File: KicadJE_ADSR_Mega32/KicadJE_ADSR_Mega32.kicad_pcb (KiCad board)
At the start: 2 copper layers, 100 x 100 mm, 134 parts, among them J101 ADSR1, J102 ADSR2, J103 ADSR1, J104 ADSR2, J105 ADSR1-G8, J106 ADSR2-G8, J107 ADSR4-G8, J108 ADSR3-G8, J201 AVR-ISP-6, J202 UART, J301 In, J302 +5V reg/doepfer, J303 Out, J304 CV_time, J305 CV doepfer, P101 Doepfer_Power_16pin, P302 Doepfer_Power_16pin, Q301 BC337, Q302 PZT2222A, U201 ATmega32A-AU, U301 L78L05_TO92, U302 PT2399, Y201 16MHz

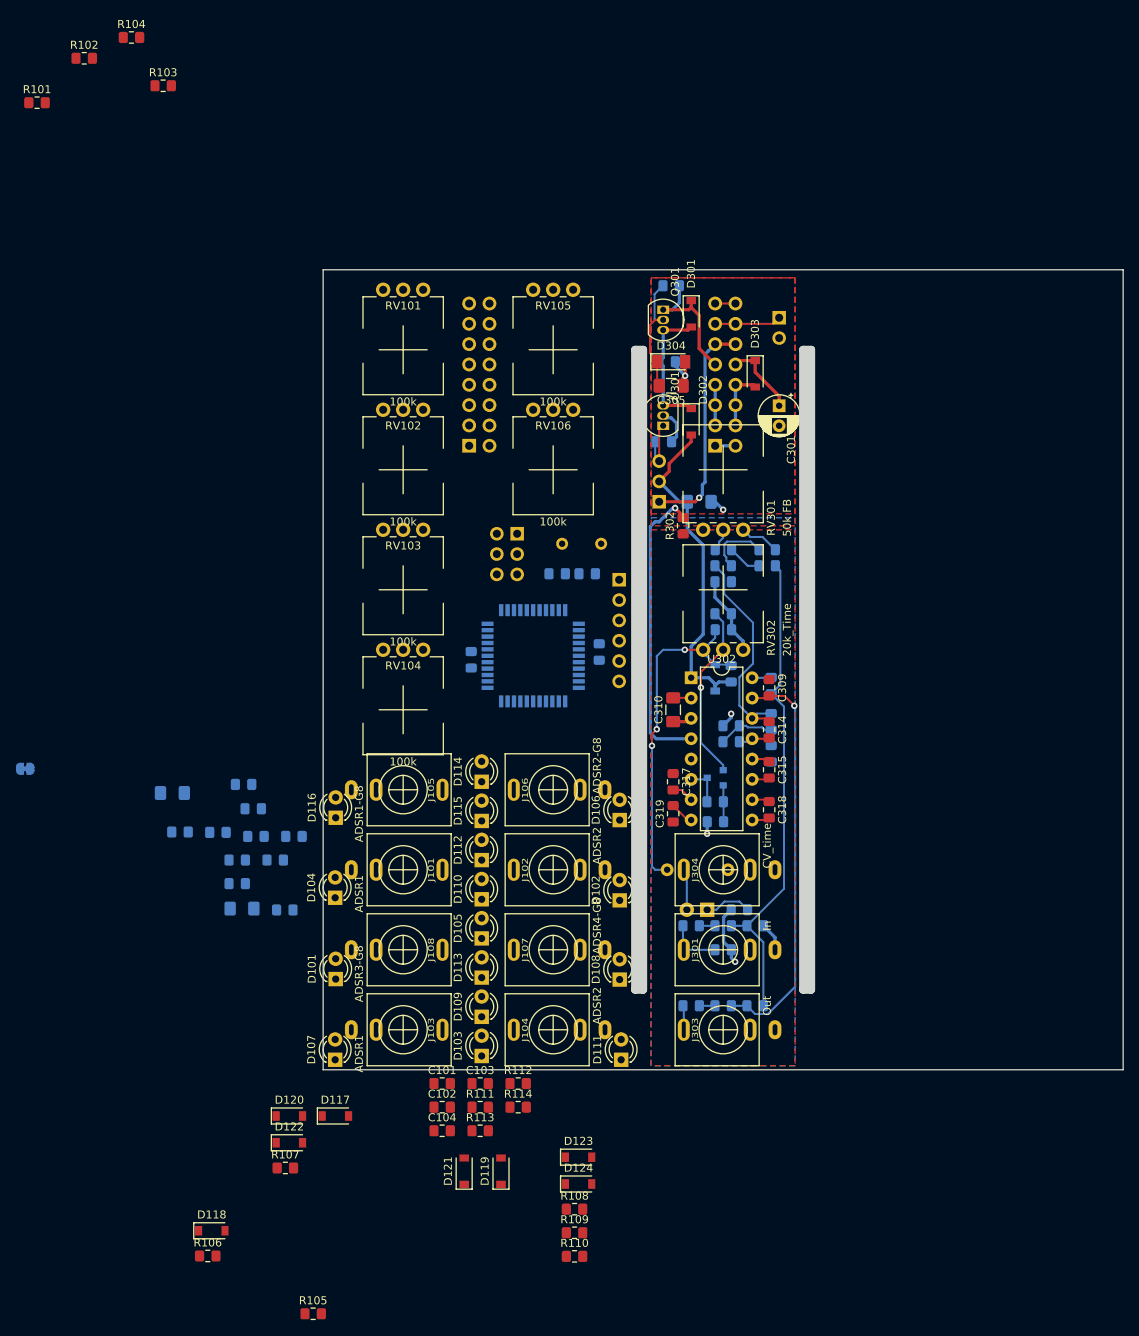
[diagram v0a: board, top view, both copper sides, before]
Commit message: Alternative pull down
Pull down via 10k but connected via TN - so if no input is applied they are connected via Gate input. This enables sync gate
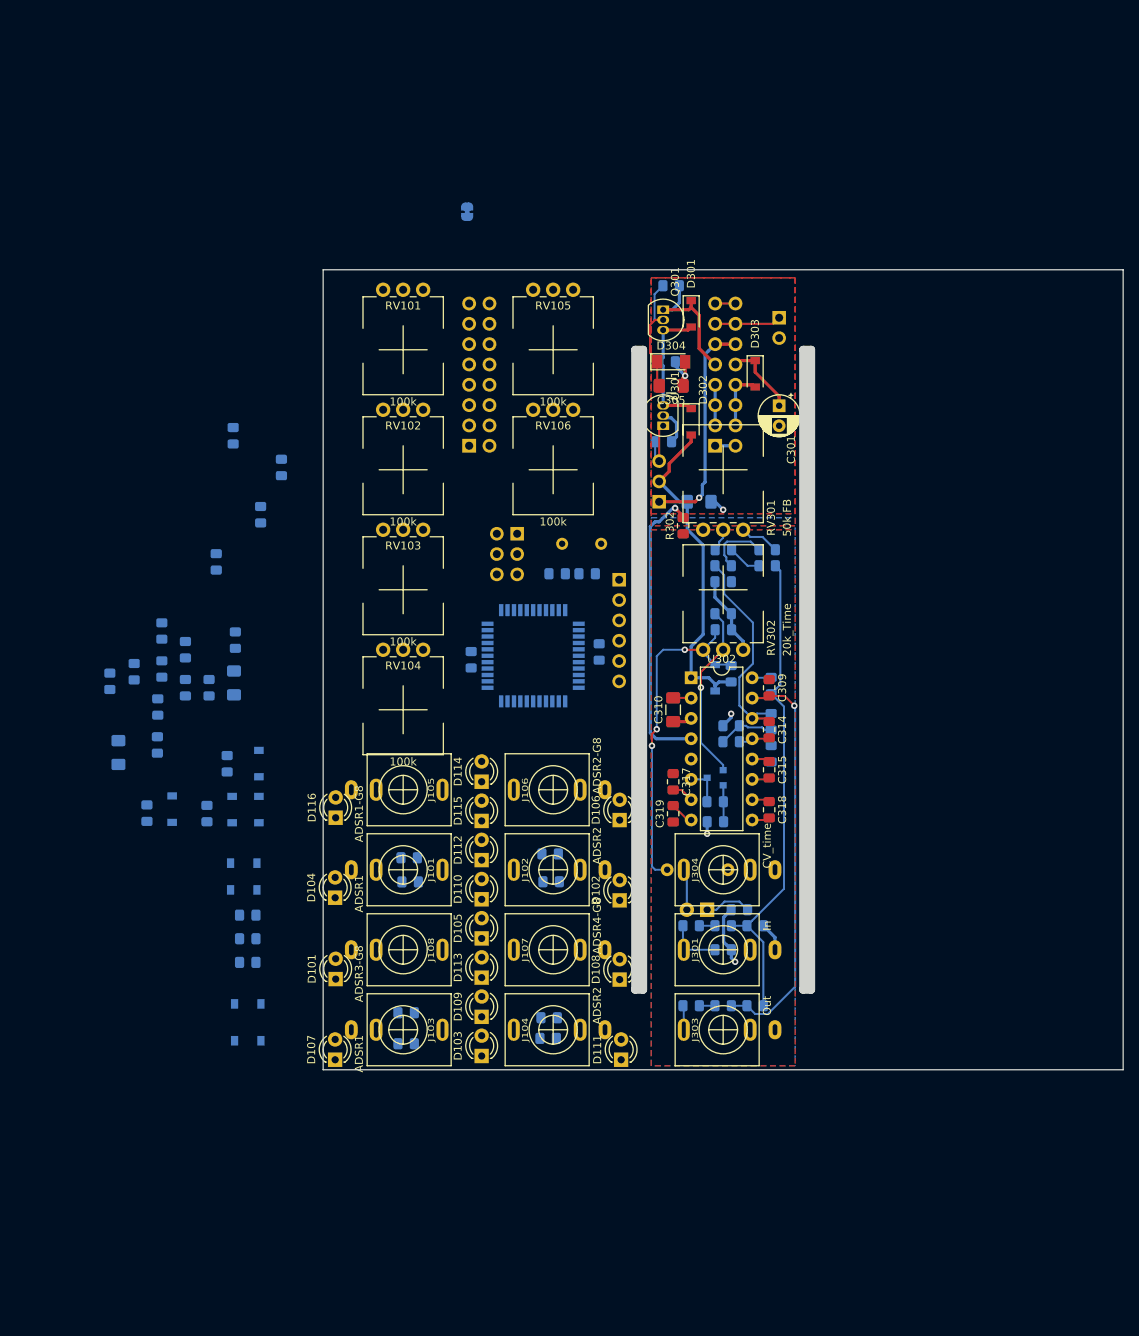
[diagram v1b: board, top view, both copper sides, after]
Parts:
- C101, C102, C103, C104, D117, D118, D119, D120, D121, D122, D123, D124, R101, R102, R103, R104, R105, R106, R107, R108, R109, R110, R111, R112, R113, R114: moved to B.Cu
- moved R204 88.9 mm to (68.0, 42.8), turned to 90 degrees
- moved R105 69.6 mm to (38.0, 111.8), turned to 90 degrees
- moved R101 61.6 mm to (36.6, 86.5), turned to 90 degrees
- moved R102 61.2 mm to (42.2, 80.6), turned to 90 degrees
- moved R104 56.9 mm to (44.8, 74.7), turned to 90 degrees
- moved R106 55.9 mm to (28.0, 117.9), turned to 90 degrees
- moved D123 55.7 mm to (40.1, 124.2), turned to 180 degrees
- moved D124 55.7 mm to (40.1, 127.5), turned to 180 degrees
- moved R108 54.9 mm to (40.6, 130.7), turned to 180 degrees
- moved R109 54.9 mm to (40.6, 133.6), turned to 180 degrees
- moved R110 54.9 mm to (40.6, 136.6), turned to 180 degrees
- moved D118 52.9 mm to (31.1, 117.4), turned to 90 degrees
- moved R107 45.4 mm to (35.5, 118.0), turned to 90 degrees
- moved D117 45.1 mm to (42.0, 111.7), turned to 90 degrees
- moved R103 44.6 mm to (38.8, 70.8), turned to 90 degrees
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
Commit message: Update KicadJE_ADSR_Mega32.kicad_pcb
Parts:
- C211, D201, R202, R204: moved to F.Cu
- moved C208 70.2 mm to (67.2, 39.5)
- moved C205 67.3 mm to (73.5, 64.3)
- moved C206 65.3 mm to (71.2, 39.5)
- moved R204 59.3 mm to (76.0, 101.5), turned to 0 degrees
- moved R201 53.6 mm to (76.2, 110.0), turned to 180 degrees
- moved R101 51.4 mm to (83.0, 108.8), turned to 270 degrees
- moved R203 50.5 mm to (76.2, 108.0), turned to 180 degrees
- moved D201 49.6 mm to (77.4, 97.5), turned to 180 degrees
- moved R102 47.9 mm to (81.0, 108.8), turned to 270 degrees
- moved C211 47.9 mm to (77.5, 85.0)
- moved R205 47.4 mm to (75.8, 88.0), turned to 180 degrees
- moved C207 47.4 mm to (73.5, 69.2), turned to 270 degrees
- moved C204 46.9 mm to (76.2, 106.0), turned to 0 degrees
- moved R103 45.4 mm to (63.2, 109.0), turned to 270 degrees
- moved D121 44.7 mm to (30.8, 102.8)
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
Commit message: Update KicadJE_ADSR_Mega32.kicad_pcb
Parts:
- moved D123 49.5 mm to (78.6, 138.0)
- moved D124 49.5 mm to (78.6, 135.5)
- moved D120 47.9 mm to (78.6, 115.0)
- moved D119 47.9 mm to (78.6, 117.5)
- moved D122 44.9 mm to (60.9, 138.0)
- moved D121 44.5 mm to (60.9, 135.5)
- moved R108 43.7 mm to (78.1, 132.2)
- moved R106 43.4 mm to (78.1, 112.5)
- moved R107 38.0 mm to (60.4, 133.2)
- moved D117 30.6 mm to (60.9, 118.0)
- moved D118 30.6 mm to (60.9, 115.8)
- moved R105 25.3 mm to (60.4, 113.5)
- moved R109 4.03 mm to (60.4, 126.8)
- moved C101 2.33 mm to (60.4, 124.2)
- moved R111 1.79 mm to (60.4, 121.8)
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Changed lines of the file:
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@@
   )
   (module Diode_SMD:D_SOD-123 (layer B.Cu)
-    (at 30.75 112.75)
+    (at 60.875001 118)
     (descr SOD-123)
     (tags SOD-123)
@@
   )
   (module Diode_SMD:D_SOD-123 (layer B.Cu)
-    (at 30.75 110.5 180)
+    (at 60.875001 115.75 180)
     (descr SOD-123)
     (tags SOD-123)
@@
   )
   (module Diode_SMD:D_SOD-123 (layer B.Cu)
-    (at 30.75 119.5)
+    (at 78.625001 117.5)
     (descr SOD-123)
     (tags SOD-123)
@@
   )
   (module Diode_SMD:D_SOD-123 (layer B.Cu)
-    (at 30.75 117.25 180)
+    (at 78.625001 115 180)
     (descr SOD-123)
     (tags SOD-123)
@@
   )
   (module Diode_SMD:D_SOD-123 (layer B.Cu)
-    (at 30.75 102.75)
+    (at 60.875001 135.525)
     (descr SOD-123)
     (tags SOD-123)
@@
   )
   (module Diode_SMD:D_SOD-123 (layer B.Cu)
-    (at 30.75 104.75 180)
+    (at 60.875001 138 180)
     (descr SOD-123)
     (tags SOD-123)
@@
   )
   (module Resistor_SMD:R_0805_2012Metric_Pad1.15x1.40mm_HandSolder (layer B.Cu)
-    (at 35.25 110.5 180)
+    (at 60.375001 113.5 180)
     (descr "Resistor SMD 0805 (2012 Metric), square (rectangular) end terminal, IPC_7351 nominal with elongated pad for handsoldering. (Body size source: https://docs.google.com/spreadsheets/d/1BsfQQcO9C6DZCsRaXUlFlo91Tg2WpOkGARC1WS5S8t0/edit?usp=sharing), generated with kicad-footprint-generator")
     (tags "resistor handsolder")
@@
   )
   (module Resistor_SMD:R_0805_2012Metric_Pad1.15x1.40mm_HandSolder (layer B.Cu)
-    (at 35 117.25 180)
+    (at 78.125001 112.5 180)
     (descr "Resistor SMD 0805 (2012 Metric), square (rectangular) end terminal, IPC_7351 nominal with elongated pad for handsoldering. (Body size source: https://docs.google.com/spreadsheets/d/1BsfQQcO9C6DZCsRaXUlFlo91Tg2WpOkGARC1WS5S8t0/edit?usp=sharing), generated with kicad-footprint-generator")
     (tags "resistor handsolder")
@@
   )
   (module Resistor_SMD:R_0805_2012Metric_Pad1.15x1.40mm_HandSolder (layer B.Cu)
-    (at 35.25 104.75 180)
+    (at 60.375001 133.25 180)
     (descr "Resistor SMD 0805 (2012 Metric), square (rectangular) end terminal, IPC_7351 nominal with elongated pad for handsoldering. (Body size source: https://docs.google.com/spreadsheets/d/1BsfQQcO9C6DZCsRaXUlFlo91Tg2WpOkGARC1WS5S8t0/edit?usp=sharing), generated with kicad-footprint-generator")
     (tags "resistor handsolder")
@@
   )
   (module Diode_SMD:D_SOD-123 (layer B.Cu)
-    (at 30.75 125.25)
+    (at 78.625001 138)
     (descr SOD-123)
     (tags SOD-123)
@@
   )
   (module Diode_SMD:D_SOD-123 (layer B.Cu)
-    (at 30.75 122.75 180)
+    (at 78.625001 135.5 180)
     (descr SOD-123)
     (tags SOD-123)
@@
   )
   (module Resistor_SMD:R_0805_2012Metric_Pad1.15x1.40mm_HandSolder (layer B.Cu)
-    (at 35 125.25 180)
+    (at 78.125001 132.25 180)
     (descr "Resistor SMD 0805 (2012 Metric), square (rectangular) end terminal, IPC_7351 nominal with elongated pad for handsoldering. (Body size source: https://docs.google.com/spreadsheets/d/1BsfQQcO9C6DZCsRaXUlFlo91Tg2WpOkGARC1WS5S8t0/edit?usp=sharing), generated with kicad-footprint-generator")
     (tags "resistor handsolder")
@@
   )
   (module Resistor_SMD:R_0805_2012Metric_Pad1.15x1.40mm_HandSolder (layer B.Cu)
-    (at 58 130 180)
+    (at 60.375001 126.75 180)
     (descr "Resistor SMD 0805 (2012 Metric), square (rectangular) end terminal, IPC_7351 nominal with elongated pad for handsoldering. (Body size source: https://docs.google.com/spreadsheets/d/1BsfQQcO9C6DZCsRaXUlFlo91Tg2WpOkGARC1WS5S8t0/edit?usp=sharing), generated with kicad-footprint-generator")
     (tags "resistor handsolder")
@@
   )
   (module Resistor_SMD:R_0805_2012Metric_Pad1.15x1.40mm_HandSolder (layer B.Cu)
-    (at 83.75 132 180)
+    (at 83.75 132.25 180)
     (descr "Resistor SMD 0805 (2012 Metric), square (rectangular) end terminal, IPC_7351 nominal with elongated pad for handsoldering. (Body size source: https://docs.google.com/spreadsheets/d/1BsfQQcO9C6DZCsRaXUlFlo91Tg2WpOkGARC1WS5S8t0/edit?usp=sharing), generated with kicad-footprint-generator")
     (tags "resistor handsolder")
@@
   )
   (module Capacitor_SMD:C_0805_2012Metric_Pad1.15x1.40mm_HandSolder (layer B.Cu)
-    (at 60.875001 126.524999)
+    (at 60.375001 124.25)
     (descr "Capacitor SMD 0805 (2012 Metric), square (rectangular) end terminal, IPC_7351 nominal with elongated pad for handsoldering. (Body size source: https://docs.google.com/spreadsheets/d/1BsfQQcO9C6DZCsRaXUlFlo91Tg2WpOkGARC1WS5S8t0/edit?usp=sharing), generated with kicad-footprint-generator")
     (tags "capacitor handsolder")
@@
   )
   (module Capacitor_SMD:C_0805_2012Metric_Pad1.15x1.40mm_HandSolder (layer B.Cu)
-    (at 78.5 126.5)
+    (at 78.125001 126.5)
     (descr "Capacitor SMD 0805 (2012 Metric), square (rectangular) end terminal, IPC_7351 nominal with elongated pad for handsoldering. (Body size source: https://docs.google.com/spreadsheets/d/1BsfQQcO9C6DZCsRaXUlFlo91Tg2WpOkGARC1WS5S8t0/edit?usp=sharing), generated with kicad-footprint-generator")
     (tags "capacitor handsolder")
@@
   )
   (module Capacitor_SMD:C_0805_2012Metric_Pad1.15x1.40mm_HandSolder (layer B.Cu)
-    (at 78.25 143.5)
+    (at 78.125001 143.5)
     (descr "Capacitor SMD 0805 (2012 Metric), square (rectangular) end terminal, IPC_7351 nominal with elongated pad for handsoldering. (Body size source: https://docs.google.com/spreadsheets/d/1BsfQQcO9C6DZCsRaXUlFlo91Tg2WpOkGARC1WS5S8t0/edit?usp=sharing), generated with kicad-footprint-generator")
     (tags "capacitor handsolder")
@@
   )
   (module Resistor_SMD:R_0805_2012Metric_Pad1.15x1.40mm_HandSolder (layer B.Cu)
-    (at 60.75 123.5)
+    (at 60.375001 121.75)
     (descr "Resistor SMD 0805 (2012 Metric), square (rectangular) end terminal, IPC_7351 nominal with elongated pad for handsoldering. (Body size source: https://docs.google.com/spreadsheets/d/1BsfQQcO9C6DZCsRaXUlFlo91Tg2WpOkGARC1WS5S8t0/edit?usp=sharing), generated with kicad-footprint-generator")
     (tags "resistor handsolder")
@@
   )
   (module Resistor_SMD:R_0805_2012Metric_Pad1.15x1.40mm_HandSolder (layer B.Cu)
-    (at 78.375001 123.024999)
+    (at 78.125001 123.024999)
     (descr "Resistor SMD 0805 (2012 Metric), square (rectangular) end terminal, IPC_7351 nominal with elongated pad for handsoldering. (Body size source: https://docs.google.com/spreadsheets/d/1BsfQQcO9C6DZCsRaXUlFlo91Tg2WpOkGARC1WS5S8t0/edit?usp=sharing), generated with kicad-footprint-generator")
     (tags "resistor handsolder")

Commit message: Update KicadJE_ADSR_Mega32.kicad_pcb
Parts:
- C202, R205: moved to F.Cu
- moved C202 0.75 mm to (75.0, 90.5)
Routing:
- net reset: track 0.00 -> 13.6 mm, vias 0 -> 1
- net Net-(C209-Pad1): track 0.00 -> 12.8 mm
- net Net-(C211-Pad2): track 0.00 -> 11.5 mm
- net GND: track 61.6 -> 71.2 mm, vias 3 -> 5
- net Net-(C210-Pad1): track 0.00 -> 9.47 mm
- net 8_Rx: track 0.00 -> 9.47 mm
- net +5V: track 27.8 -> 36.8 mm, vias 1 -> 2
- net 9_Tx: track 0.00 -> 9.01 mm

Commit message: power routing
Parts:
- moved C208 30.0 mm to (66.0, 69.5), turned to 270 degrees
- moved C206 26.5 mm to (66.0, 65.5)
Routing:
- net +5V: track 36.8 -> 150.9 mm
- net 24_A0: track 0.00 -> 56.9 mm
- net 25_A1: track 0.00 -> 53.3 mm
- net 26_A2: track 0.00 -> 31.5 mm, vias 0 -> 2
- net 7_SCK: track 0.00 -> 18.1 mm
- net 6_MISO: track 0.00 -> 11.3 mm
- net GND: track 71.2 -> 81.3 mm, vias 5 -> 6
- net reset: track 13.6 -> 23.5 mm
- net 5_MOSI: track 0.00 -> 9.87 mm
- net GNDA: track 26.9 -> 33.6 mm, vias 3 -> 4
- net +5VA: track 41.9 -> 48.0 mm
- net 0_LED: track 0.00 -> 1.95 mm, vias 0 -> 1
- net Net-(D201-Pad2): track 0.00 -> 1.86 mm
- net 8_Rx: track 9.47 -> 10.6 mm
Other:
- net class Default: trace_width 0.25 -> 0.2

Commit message: Prior to turning Atmega32
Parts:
- moved R103 8.02 mm to (71.2, 108.5)
- moved R104 3.29 mm to (68.5, 108.5)
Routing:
- net 19: track 0.00 -> 40.2 mm, vias 0 -> 4
- net 21: track 0.00 -> 35.9 mm, vias 0 -> 2
- net +5V: track 150.9 -> 185.4 mm
- net Net-(D101-Pad1): track 0.00 -> 33.3 mm, vias 0 -> 4
- net 11_INT1: track 0.00 -> 31.4 mm
- net 18: track 0.00 -> 28.5 mm, vias 0 -> 2
- net Net-(D102-Pad1): track 0.00 -> 24.9 mm, vias 0 -> 2
- net 27_A3: track 0.00 -> 15.8 mm, vias 0 -> 2
- net Net-(D103-Pad1): track 0.00 -> 9.97 mm
- net 22: track 0.00 -> 6.31 mm
- net 23: track 0.00 -> 5.08 mm
- net ADSR2-G8: track 0.00 -> 4.69 mm
- net 8_Rx: track 10.6 -> 14.7 mm
- net GND: track 81.3 -> 83.9 mm
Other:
- net class Default: clearance 0.2 -> 0.15; via_dia 0.8 -> 0.7
- rule trace_clearance: 0.2 -> 0.15

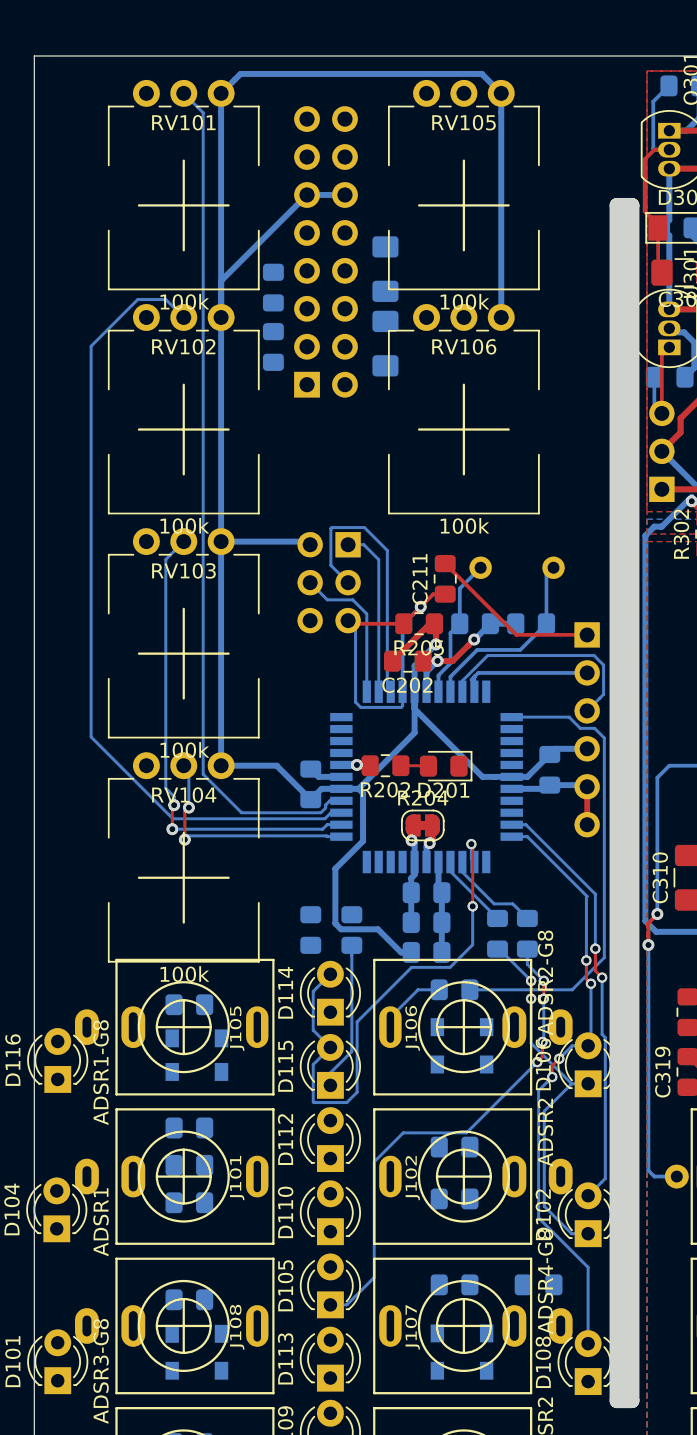
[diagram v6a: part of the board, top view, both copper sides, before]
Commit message: Atmega rotated
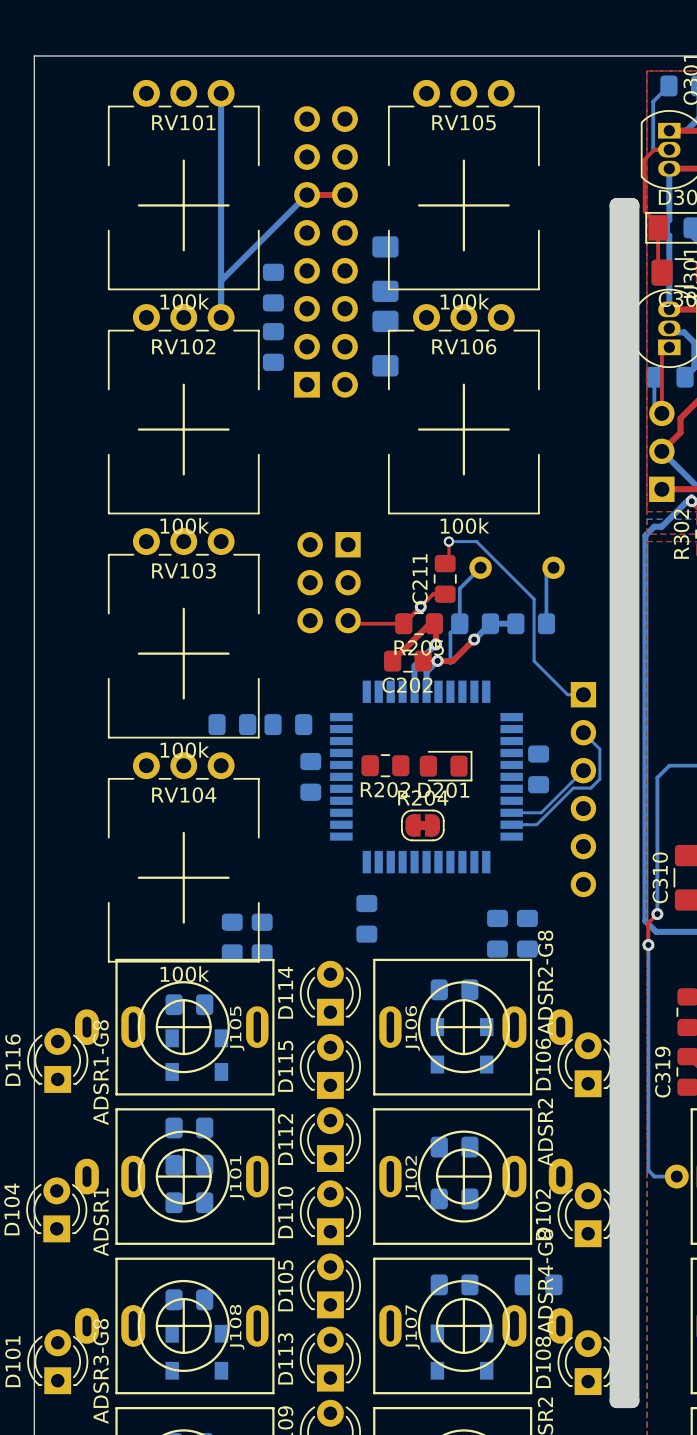
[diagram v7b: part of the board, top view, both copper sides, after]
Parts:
- moved R201 20.0 mm to (63.2, 94.8)
- moved R203 16.2 mm to (67.0, 94.8), turned to 0 degrees
- moved C204 11.0 mm to (68.5, 98.2), turned to 270 degrees
- moved C203 9.75 mm to (72.2, 107.8)
- moved R103 8.02 mm to (63.2, 109.0)
- moved J202 4.01 mm to (86.8, 92.8)
- moved R104 3.29 mm to (65.2, 109.0)
- moved C201 0.75 mm to (83.8, 97.8)
- turned U201 to 180 degrees
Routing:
- net +5V: track 185.4 -> 64.9 mm
- net 24_A0: track 56.9 -> 0.00 mm
- net 25_A1: track 53.3 -> 0.00 mm
- net 19: track 40.2 -> 0.00 mm, vias 4 -> 0
- net 21: track 35.9 -> 0.00 mm, vias 2 -> 0
- net Net-(D101-Pad1): track 33.3 -> 0.00 mm, vias 4 -> 0
- net 26_A2: track 31.5 -> 0.00 mm, vias 2 -> 0
- net 11_INT1: track 31.4 -> 0.00 mm
- net 18: track 28.5 -> 0.00 mm, vias 2 -> 0
- net Net-(D102-Pad1): track 24.9 -> 0.00 mm, vias 2 -> 0
- net 7_SCK: track 18.1 -> 0.00 mm
- net 27_A3: track 15.8 -> 0.00 mm, vias 2 -> 0
- net reset: track 23.5 -> 9.12 mm
- net GND: track 83.9 -> 71.2 mm, vias 6 -> 5
- net 6_MISO: track 11.3 -> 0.00 mm
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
